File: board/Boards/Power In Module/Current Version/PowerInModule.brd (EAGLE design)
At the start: 25.4 x 30.1 mm, 10 parts

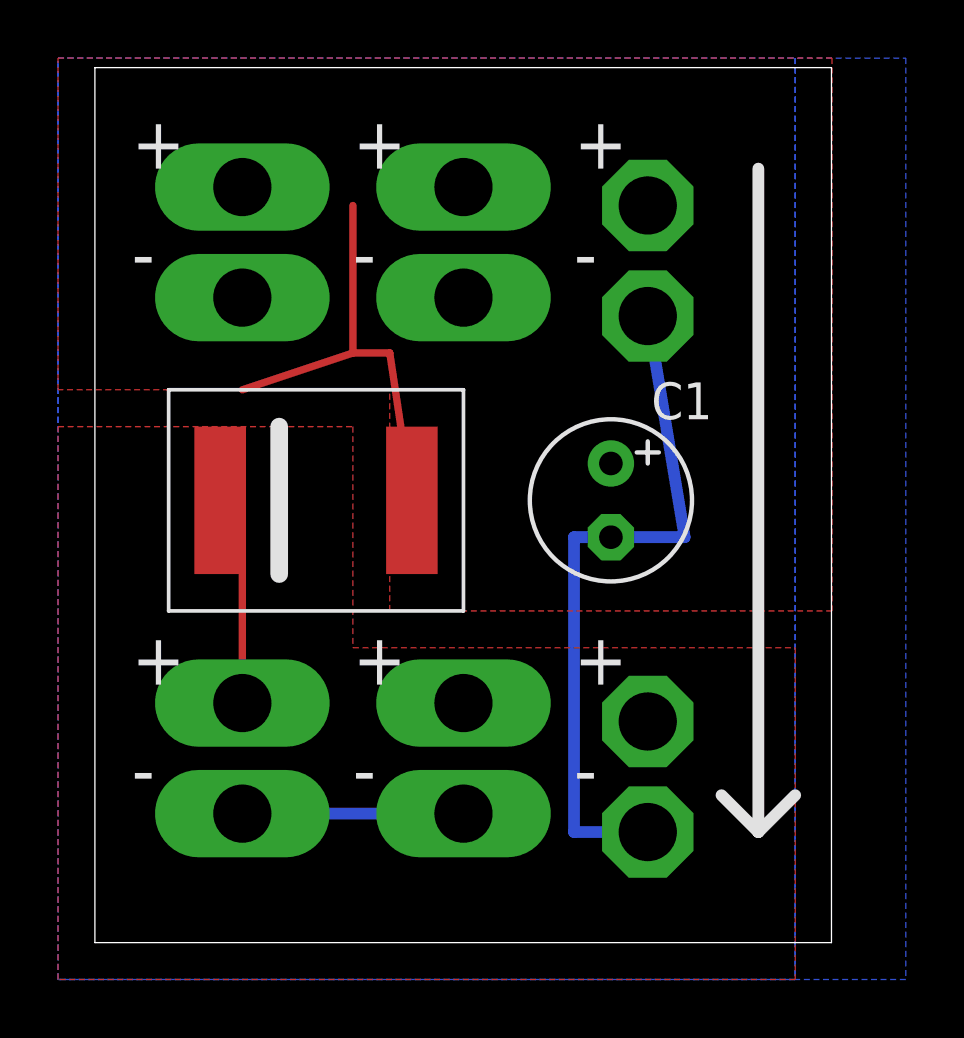
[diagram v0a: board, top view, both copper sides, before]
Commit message: fixed "thermals"
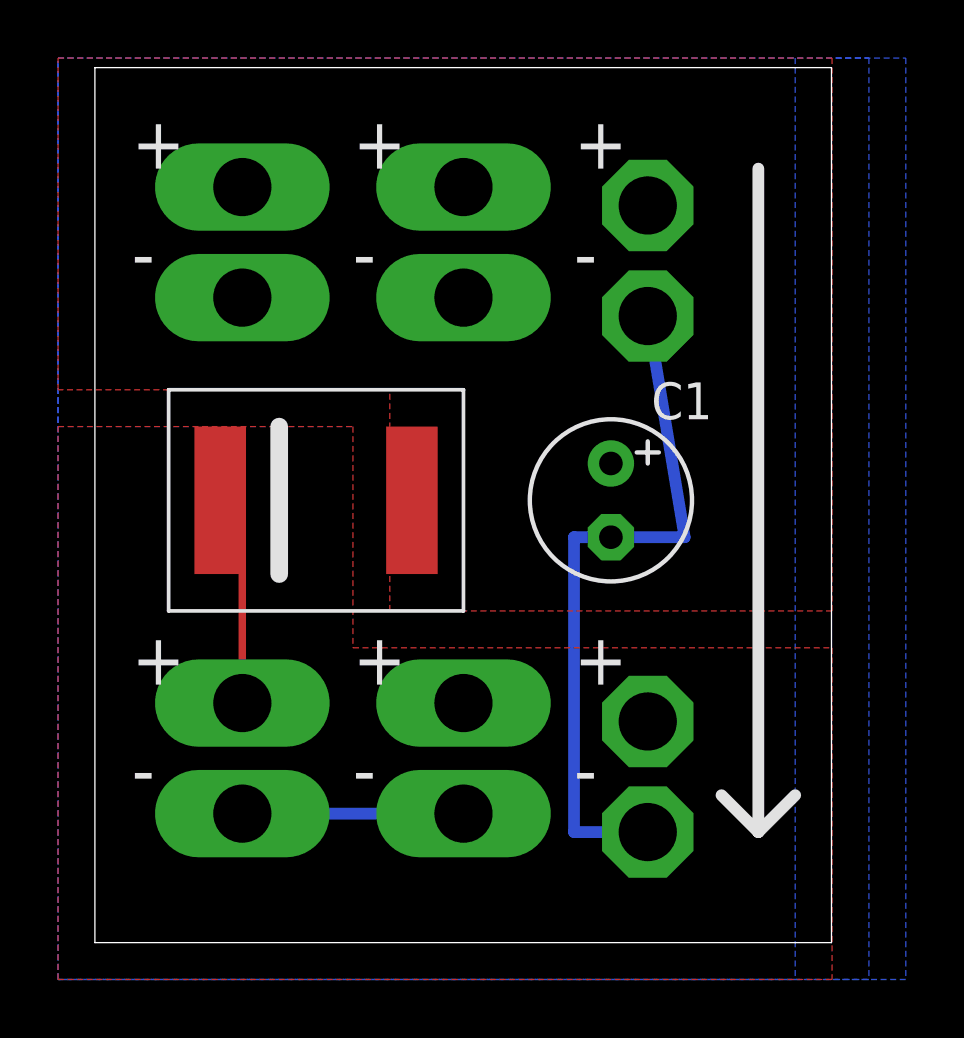
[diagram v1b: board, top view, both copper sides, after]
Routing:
- net N$1: track 17.3 -> 3.15 mm
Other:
- board text added: "PwrModule v1.0 hitchBOT C.G and D.K August 2014"
- board text removed: "PwrModule v1.0 C.G and D.K August 2014"
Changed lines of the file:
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@@
 <setting verticaltext="up"/>
 </settings>
-<grid distance="0.05" unitdist="inch" unit="inch" style="lines" multiple="1" display="no" altdistance="0.025" altunitdist="inch" altunit="inch"/>
+<grid distance="0.1" unitdist="mm" unit="mm" style="lines" multiple="1" display="yes" altdistance="0.025" altunitdist="inch" altunit="inch"/>
 <layers>
 <layer number="1" name="Top" color="4" fill="1" visible="yes" active="yes"/>
@@
 <wire x1="22.86" y1="3.81" x2="21.59" y2="5.08" width="0.4064" layer="21"/>
 <wire x1="22.86" y1="3.81" x2="24.13" y2="5.08" width="0.4064" layer="21"/>
-<text x="15.24" y="13.97" size="1.2446" layer="22" rot="MR0">PwrModule v1.0
+<text x="15.24" y="12.7" size="1.2446" layer="22" rot="MR0">PwrModule v1.0
+hitchBOT
 C.G and D.K
 August 2014</text>
@@
 <wire x1="12.7" y1="3.81" x2="12.7" y2="4.445" width="0.4064" layer="16"/>
 <wire x1="12.7" y1="4.445" x2="5.08" y2="4.445" width="0.4064" layer="16"/>
-<polygon width="0.4064" layer="16" isolate="0.4064">
+<polygon width="0.4064" layer="16" isolate="0.4064" thermals="no">
 <vertex x="-1.27" y="30.48"/>
-<vertex x="24.13" y="30.48"/>
-<vertex x="24.13" y="-1.27"/>
+<vertex x="26.67" y="30.48"/>
+<vertex x="26.67" y="-1.27"/>
 <vertex x="-1.27" y="-1.27"/>
 </polygon>
@@
 <wire x1="11.43" y1="15.24" x2="11.43" y2="16.51" width="0.254" layer="1"/>
 <wire x1="11.43" y1="15.24" x2="10.922" y2="15.24" width="0.254" layer="1"/>
-<wire x1="8.89" y1="20.32" x2="8.89" y2="25.4" width="0.254" layer="1"/>
-<wire x1="10.16" y1="20.32" x2="8.89" y2="20.32" width="0.254" layer="1"/>
-<wire x1="8.89" y1="20.32" x2="5.08" y2="19.05" width="0.254" layer="1"/>
-<wire x1="10.16" y1="20.32" x2="10.922" y2="15.24" width="0.254" layer="1"/>
-<polygon width="0.4064" layer="1" isolate="0.4064">
+<wire x1="11.43" y1="16.51" x2="10.922" y2="15.24" width="0.254" layer="1"/>
+<polygon width="0.4064" layer="1" isolate="0.4064" thermals="no">
 <vertex x="-1.27" y="30.48"/>
 <vertex x="25.4" y="30.48"/>
@@
 <wire x1="12.7" y1="8.89" x2="12.7" y2="8.255" width="0.254" layer="1"/>
 <wire x1="19.05" y1="8.255" x2="19.05" y2="7.62" width="0.4064" layer="1"/>
-<polygon width="0.4064" layer="1" isolate="0.4064">
+<polygon width="0.4064" layer="1" isolate="0.4064" thermals="no">
 <vertex x="-1.27" y="17.78"/>
 <vertex x="8.89" y="17.78"/>
 <vertex x="8.89" y="10.16"/>
-<vertex x="24.13" y="10.16"/>
-<vertex x="24.13" y="-1.27"/>
+<vertex x="25.4" y="10.16"/>
+<vertex x="25.4" y="-1.27"/>
 <vertex x="-1.27" y="-1.27"/>
 </polygon>
